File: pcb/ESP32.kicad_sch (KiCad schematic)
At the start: 27 parts, among them J5 SPKR, SW1 BOOT, SW2 RESET, U3 SN74LV1T34DBV, U5 MAX98357A, U8 ESP32-S3-WROOM-2-N32R16V

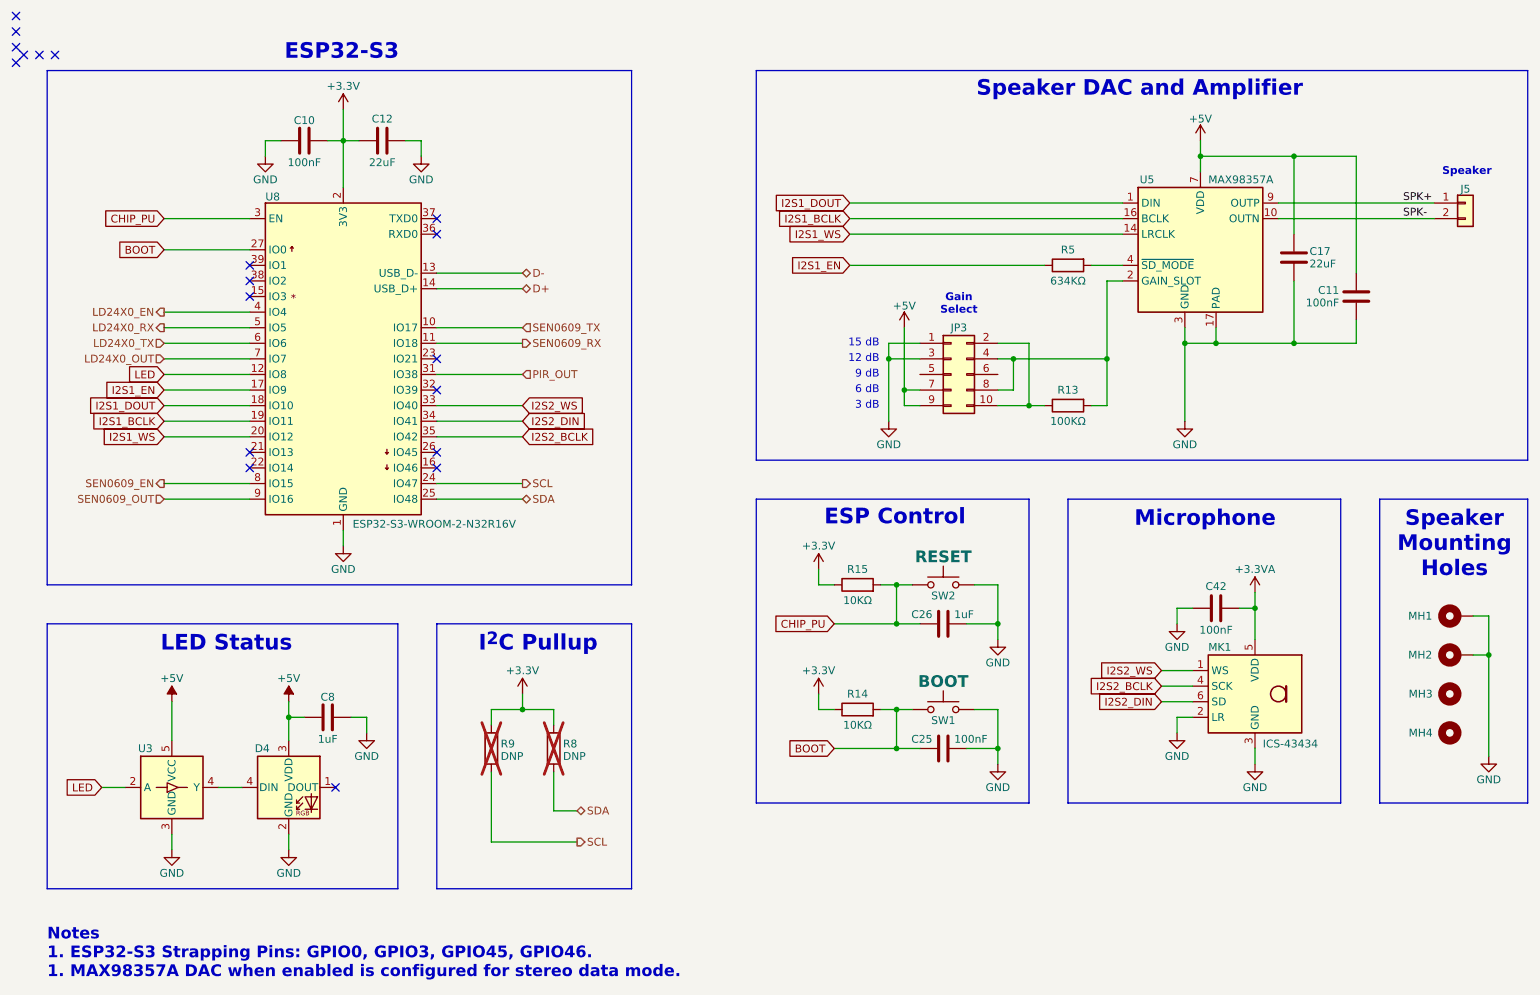
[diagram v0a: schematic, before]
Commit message: Minor changes
Separate SEN66 on a separate I2C bus.
Add WIFi Antenna cutout.
Beef-up Power and Ground connections to SEN66.
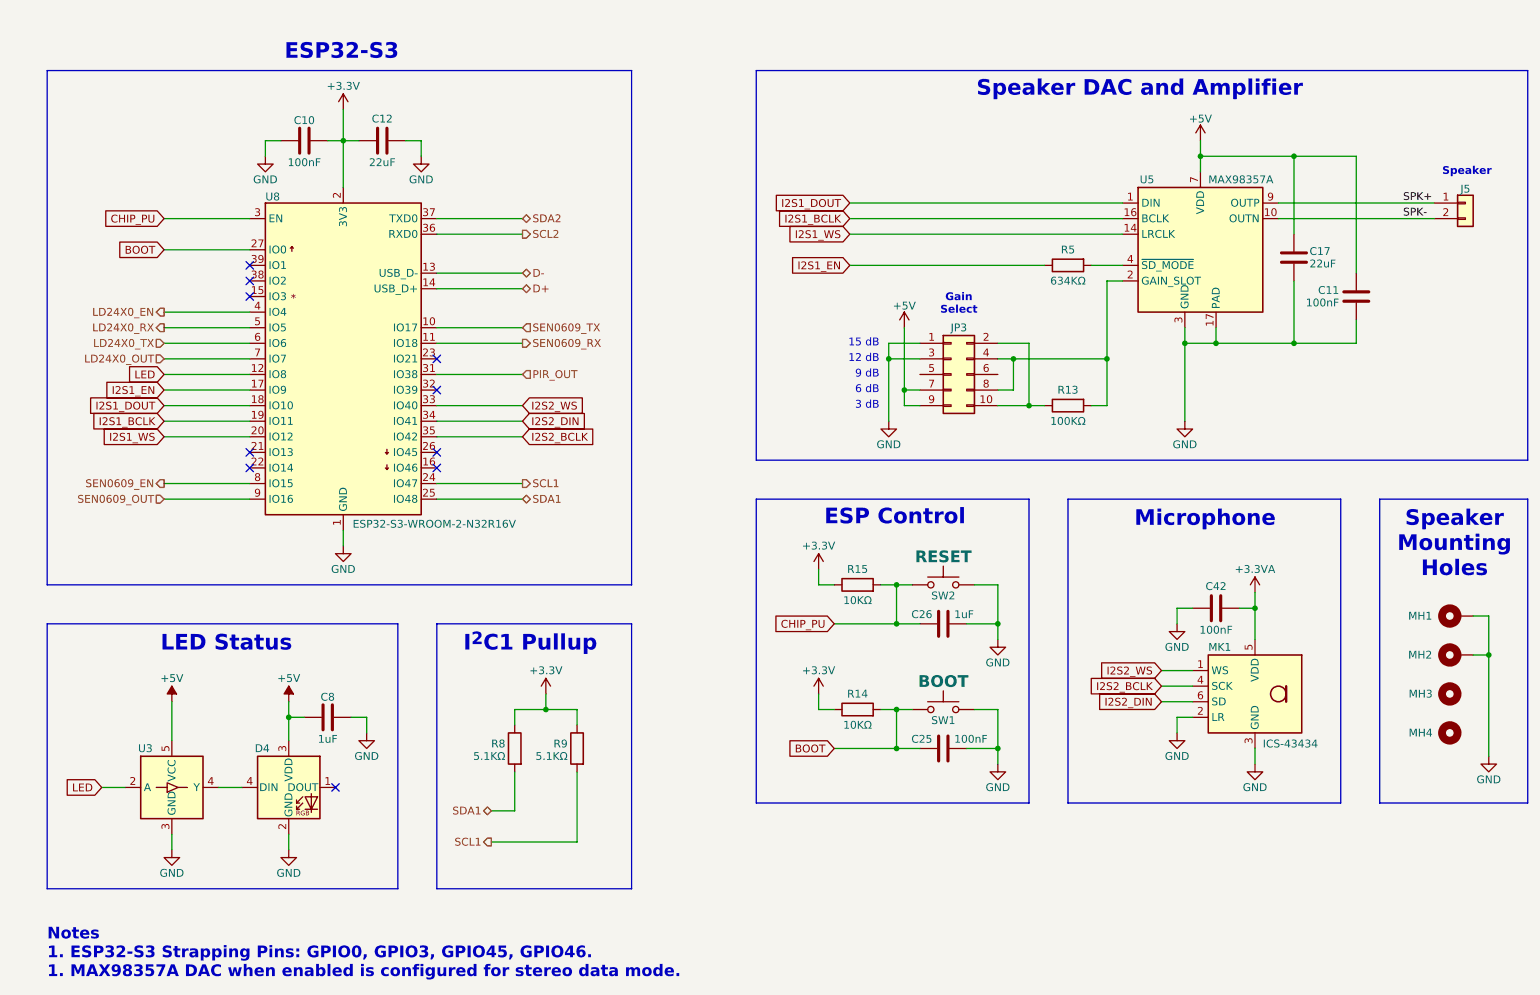
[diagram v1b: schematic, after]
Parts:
- R8, R9: value DNP -> 5.1KΩ; Manufacturer (none) -> Vishay / Dale; Part Number (none) -> CRCW04025K10FKED; now fitted
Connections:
- net SCL2: now reaches U8.36 (RXD0)
- net SDA2: now reaches U8.37 (TXD0)
- net SCL renamed SCL1
- net SDA renamed SDA1
- no-connect marks 19 -> 10
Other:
- note added: "I^{2}C1 Pullup"
- note removed: "I^{2}C Pullup"
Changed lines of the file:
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@@
 	(title_block
 		(title "ESPHome Parking Assistant")
-		(date "2025-04-10")
-		(rev "-")
+		(date "2025-04-18")
+		(rev "A")
 		(company "Mike Lawrence")
 	)
@@
 	)
 	(rectangle
-		(start 88.9 115.57)
-		(end 120.65 158.75)
+		(start 120.65 115.57)
+		(end 88.9 158.75)
 		(stroke
 			(width 0)
@@
 		)
 	)
-	(text "I^{2}C Pullup"
+	(text "I^{2}C1 Pullup"
 		(exclude_from_sim no)
-		(at 105.41 117.348 0)
+		(at 104.14 117.348 0)
 		(effects
 			(font
@@
 	)
 	(junction
-		(at 102.87 129.54)
+		(at 106.68 129.54)
 		(diameter 0)
 		(color 0 0 0 0)
@@
 	)
 	(no_connect
-		(at 26.67 22.86)
-	)
-	(no_connect
 		(at 58.42 62.23)
 	)
@@
 	)
 	(no_connect
-		(at 88.9 49.53)
-	)
-	(no_connect
 		(at 88.9 90.17)
 	)
 	(no_connect
-		(at 20.32 24.13)
-	)
-	(no_connect
-		(at 20.32 19.05)
-	)
-	(no_connect
-		(at 24.13 22.86)
-	)
-	(no_connect
-		(at 21.59 22.86)
-	)
-	(no_connect
 		(at 58.42 90.17)
 	)
@@
 		(at 58.42 59.69)
 	)
-	(no_connect
-		(at 88.9 52.07)
-	)
-	(no_connect
-		(at 20.32 21.59)
-	)
-	(no_connect
-		(at 20.32 16.51)
-	)
 	(wire
 		(pts
@@
 	(wire
 		(pts
-			(xy 102.87 129.54) (xy 107.95 129.54)
+			(xy 106.68 129.54) (xy 101.6 129.54)
 		)
 		(stroke
@@
 	(wire
 		(pts
-			(xy 107.95 146.05) (xy 111.76 146.05)
+			(xy 101.6 146.05) (xy 97.79 146.05)
 		)
 		(stroke
@@
 	(wire
 		(pts
-			(xy 107.95 139.7) (xy 107.95 146.05)
+			(xy 101.6 139.7) (xy 101.6 146.05)
 		)
 		(stroke
@@
 	(wire
 		(pts
-			(xy 97.79 129.54) (xy 102.87 129.54)
+			(xy 111.76 129.54) (xy 106.68 129.54)
 		)
 		(stroke
@@
 	(wire
 		(pts
-			(xy 102.87 127) (xy 102.87 129.54)
+			(xy 106.68 127) (xy 106.68 129.54)
 		)
 		(stroke
@@
 	(wire
 		(pts
-			(xy 107.95 129.54) (xy 107.95 132.08)
+			(xy 101.6 129.54) (xy 101.6 132.08)
 		)
 		(stroke
@@
 	(wire
 		(pts
-			(xy 97.79 151.13) (xy 111.76 151.13)
+			(xy 111.76 151.13) (xy 97.79 151.13)
 		)
 		(stroke
@@
 	(wire
 		(pts
-			(xy 97.79 139.7) (xy 97.79 151.13)
+			(xy 111.76 139.7) (xy 111.76 151.13)
 		)
 		(stroke
@@
 	(wire
 		(pts
+			(xy 88.9 49.53) (xy 102.87 49.53)
+		)
+		(stroke
+			(width 0)
+			(type default)
+		)
+	)
+	(wire
+		(pts
 			(xy 260.35 120.65) (xy 260.35 137.16)
 		)
@@
 	(wire
 		(pts
-			(xy 97.79 132.08) (xy 97.79 129.54)
+			(xy 111.76 132.08) (xy 111.76 129.54)
+		)
+		(stroke
+			(width 0)
+			(type default)
+		)
+	)
+	(wire
+		(pts
+			(xy 88.9 52.07) (xy 102.87 52.07)
 		)
 		(stroke
@@
 		)
 	)
-	(hierarchical_label "SCL"
+	(hierarchical_label "SCL1"
 		(shape output)
 		(at 102.87 92.71 0)
@@
 		)
 	)
-	(hierarchical_label "SDA"
+	(hierarchical_label "SDA1"
 		(shape bidirectional)
 		(at 102.87 95.25 0)
@@
 		)
 	)
+	(hierarchical_label "SCL2"
+		(shape output)
+		(at 102.87 52.07 0)
+		(effects
+			(font
+				(size 1.27 1.27)
+			)
+			(justify left)
+		)
+	)
 	(hierarchical_label "LD24X0_RX"
 		(shape output)
@@
 		)
 	)
-	(hierarchical_label "SCL"
+	(hierarchical_label "SCL1"
 		(shape output)
-		(at 111.76 151.13 0)
+		(at 97.79 151.13 180)
 		(effects
 			(font
 				(size 1.27 1.27)
 			)
-			(justify left)
+			(justify right)
 		)
 	)
@@
 		)
 	)
+	(hierarchical_label "SDA2"
+		(shape bidirectional)
+		(at 102.87 49.53 0)
+		(effects
+			(font
+				(size 1.27 1.27)
+			)
+			(justify left)
+		)
+	)
 	(hierarchical_label "SEN0609_RX"
 		(shape output)
@@
 		)
 	)
-	(hierarchical_label "SDA"
+	(hierarchical_label "SDA1"
 		(shape bidirectional)
-		(at 111.76 146.05 0)
+		(at 97.79 146.05 180)
 		(effects
 			(font
 				(size 1.27 1.27)
 			)
-			(justify left)
+			(justify right)
 		)
 	)
@@
 	(symbol
 		(lib_id "power:+3.3VA")
-		(at 102.87 127 0)
+		(at 106.68 127 0)
+		(mirror y)
 		(unit 1)
 		(exclude_from_sim no)
@@
 		(dnp no)
 		(property "Reference" "#PWR015"
-			(at 102.87 130.81 0)
+			(at 106.68 130.81 0)
 			(effects
 				(font
@@
 		)
 		(property "Value" "+3.3V"
-			(at 102.87 123.19 0)
+			(at 106.68 123.19 0)
 			(effects
 				(font
@@
 		)
 		(property "Footprint" ""
-			(at 102.87 127 0)
+			(at 106.68 127 0)
 			(effects
 				(font
@@
 		)
 		(property "Datasheet" ""
-			(at 102.87 127 0)
+			(at 106.68 127 0)
 			(effects
 				(font
@@
 		)
 		(property "Description" "Power symbol creates a global label with name \"+3.3VA\""
-			(at 102.87 127 0)
+			(at 106.68 127 0)
 			(effects
 				(font
@@
 	(symbol
 		(lib_id "Device:R")
-		(at 97.79 135.89 0)
+		(at 111.76 135.89 0)
+		(mirror y)
 		(unit 1)
 		(exclude_from_sim no)
 		(in_bom yes)
 		(on_board yes)
-		(dnp yes)
+		(dnp no)
 		(property "Reference" "R9"
-			(at 99.314 135.128 0)
+			(at 110.236 135.128 0)
 			(effects
 				(font
@@
 			)
 		)
-		(property "Value" "DNP"
-			(at 99.314 137.16 0)
+		(property "Value" "5.1KΩ"
+			(at 110.236 137.16 0)
 			(effects
 				(font
@@
 		)
 		(property "Footprint" "Resistor_SMD:R_0402_1005Metric"
-			(at 96.012 135.89 90)
+			(at 113.538 135.89 90)
 			(effects
 				(font
@@
 		)
 		(property "Datasheet" "~"
-			(at 97.79 135.89 0)
+			(at 111.76 135.89 0)
+			(effects
+				(font
+					(size 1.27 1.27)
+				)
+				(hide yes)
+			)
+		)
+		(property "Description" "Resistor, 5.1KΩ, 62.5mW, 1%, 0402"
+			(at 111.76 135.89 0)
+			(effects
+				(font
+					(size 1.27 1.27)
+				)
+				(hide yes)
+			)
+		)
+		(property "Manufacturer" "Vishay / Dale"
+			(at 111.76 135.89 0)
 			(effects
 				(font
@@
 			)
 		)
-		(property "Description" "Resistor, Do Not Populate, 0402"
-			(at 97.79 135.89 0)
+		(property "Part Number" "CRCW04025K10FKED"
+			(at 111.76 135.89 0)
 			(effects
 				(font
@@
 	(symbol
 		(lib_id "Device:R")
-		(at 107.95 135.89 0)
+		(at 101.6 135.89 0)
+		(mirror y)
 		(unit 1)
 		(exclude_from_sim no)
 		(in_bom yes)
 		(on_board yes)
-		(dnp yes)
+		(dnp no)
 		(property "Reference" "R8"
-			(at 109.474 135.128 0)
+			(at 100.076 135.128 0)
 			(effects
 				(font
@@
 			)
 		)
-		(property "Value" "DNP"
-			(at 109.474 137.16 0)
+		(property "Value" "5.1KΩ"
+			(at 100.076 137.16 0)
 			(effects
 				(font
@@
 		)
 		(property "Footprint" "Resistor_SMD:R_0402_1005Metric"
-			(at 106.172 135.89 90)
+			(at 103.378 135.89 90)
 			(effects
 				(font
@@
 		)
 		(property "Datasheet" "~"
-			(at 107.95 135.89 0)
+			(at 101.6 135.89 0)
+			(effects
+				(font
+					(size 1.27 1.27)
+				)
+				(hide yes)
+			)
+		)
+		(property "Description" "Resistor, 5.1KΩ, 62.5mW, 1%, 0402"
+			(at 101.6 135.89 0)
+			(effects
+				(font
+					(size 1.27 1.27)
+				)
+				(hide yes)
+			)
+		)
+		(property "Manufacturer" "Vishay / Dale"
+			(at 101.6 135.89 0)
 			(effects
 				(font
@@
 			)
 		)
-		(property "Description" "Resistor, Do Not Populate, 0402"
-			(at 107.95 135.89 0)
+		(property "Part Number" "CRCW04025K10FKED"
+			(at 101.6 135.89 0)
 			(effects
 				(font
